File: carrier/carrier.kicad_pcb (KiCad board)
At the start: 2 copper layers, 14 x 12 mm, 2 parts, among them J1 DF40GB-30DP-0.4V(51), U1 TC58NVG1S3HBAI6

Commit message: Align net class + docs with the net names actually used
Schematic uses the datasheet slash form (/CE, /WE, /RE, /WP, RY//BY) rather
than the nCE-style placeholders I had documented. Signal class updated to
match; net-to-class patterns documented for manual entry.

Co-Authored-By: Claude Opus 5 <noreply@anthropic.com>
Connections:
- net /ALE renamed ALE
- net /CLE renamed CLE
- net /IO1 renamed IO1
- net /IO2 renamed IO2
- net /IO3 renamed IO3
- net /IO4 renamed IO4
- net /IO5 renamed IO5
- net /IO6 renamed IO6
- net /IO7 renamed IO7
- net /IO8 renamed IO8
- net /RY//BY renamed RY//BY
- net //CE renamed /CE
- net //RE renamed /RE
- net //WE renamed /WE
- net //WP renamed /WP
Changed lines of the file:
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@@
 			(size 0.23 0.66)
 			(layers "F.Cu" "F.Mask" "F.Paste")
-			(net "/IO1")
+			(net "IO1")
 			(pinfunction "1_1")
 			(pintype "passive")
@@
 			(size 0.23 0.66)
 			(layers "F.Cu" "F.Mask" "F.Paste")
-			(net "/{slash}CE")
+			(net "{slash}CE")
 			(pinfunction "4_4")
 			(pintype "passive")
@@
 			(size 0.23 0.66)
 			(layers "F.Cu" "F.Mask" "F.Paste")
-			(net "/IO2")
+			(net "IO2")
 			(pinfunction "5_5")
 			(pintype "passive")
@@
 			(size 0.23 0.66)
 			(layers "F.Cu" "F.Mask" "F.Paste")
-			(net "/CLE")
+			(net "CLE")
 			(pinfunction "8_8")
 			(pintype "passive")
@@
 			(size 0.23 0.66)
 			(layers "F.Cu" "F.Mask" "F.Paste")
-			(net "/IO3")
+			(net "IO3")
 			(pinfunction "9_9")
 			(pintype "passive")
@@
 			(size 0.23 0.66)
 			(layers "F.Cu" "F.Mask" "F.Paste")
-			(net "/ALE")
+			(net "ALE")
 			(pinfunction "12_12")
 			(pintype "passive")
@@
 			(size 0.23 0.66)
 			(layers "F.Cu" "F.Mask" "F.Paste")
-			(net "/IO4")
+			(net "IO4")
 			(pinfunction "13_13")
 			(pintype "passive")
@@
 			(size 0.23 0.66)
 			(layers "F.Cu" "F.Mask" "F.Paste")
-			(net "/{slash}WE")
+			(net "{slash}WE")
 			(pinfunction "16_16")
 			(pintype "passive")
@@
 			(size 0.23 0.66)
 			(layers "F.Cu" "F.Mask" "F.Paste")
-			(net "/IO5")
+			(net "IO5")
 			(pinfunction "17_17")
 			(pintype "passive")
@@
 			(size 0.23 0.66)
 			(layers "F.Cu" "F.Mask" "F.Paste")
-			(net "/{slash}RE")
+			(net "{slash}RE")
 			(pinfunction "20_20")
 			(pintype "passive")
@@
 			(size 0.23 0.66)
 			(layers "F.Cu" "F.Mask" "F.Paste")
-			(net "/IO6")
+			(net "IO6")
 			(pinfunction "21_21")
 			(pintype "passive")
@@
 			(size 0.23 0.66)
 			(layers "F.Cu" "F.Mask" "F.Paste")
-			(net "/{slash}WP")
+			(net "{slash}WP")
 			(pinfunction "24_24")
 			(pintype "passive")
@@
 			(size 0.23 0.66)
 			(layers "F.Cu" "F.Mask" "F.Paste")
-			(net "/IO7")
+			(net "IO7")
 			(pinfunction "25_25")
 			(pintype "passive")
@@
 			(size 0.23 0.66)
 			(layers "F.Cu" "F.Mask" "F.Paste")
-			(net "/RY{slash}{slash}BY")
+			(net "RY{slash}{slash}BY")
 			(pinfunction "28_28")
 			(pintype "passive")
@@
 			(size 0.23 0.66)
 			(layers "F.Cu" "F.Mask" "F.Paste")
-			(net "/IO8")
+			(net "IO8")
 			(pinfunction "29_29")
 			(pintype "passive")
@@
 			(size 0.4 0.4)
 			(layers "B.Cu" "B.Mask")
-			(net "/{slash}WP")
+			(net "{slash}WP")
 			(pinfunction "~{WP}_B2")
 			(pintype "input")
@@
 			(size 0.4 0.4)
 			(layers "B.Cu" "B.Mask")
-			(net "/ALE")
+			(net "ALE")
 			(pinfunction "ALE_B3")
 			(pintype "input")
@@
 			(size 0.4 0.4)
 			(layers "B.Cu" "B.Mask")
-			(net "/{slash}CE")
+			(net "{slash}CE")
 			(pinfunction "~{CE}_B5")
 			(pintype "input")
@@
 			(size 0.4 0.4)
 			(layers "B.Cu" "B.Mask")
-			(net "/{slash}WE")
+			(net "{slash}WE")
 			(pinfunction "~{WE}_B6")
 			(pintype "input")
@@
 			(size 0.4 0.4)
 			(layers "B.Cu" "B.Mask")
-			(net "/RY{slash}{slash}BY")
+			(net "RY{slash}{slash}BY")
 			(pinfunction "RY/~{BY}_B7")
 			(pintype "open_collector")
@@
 			(size 0.4 0.4)
 			(layers "B.Cu" "B.Mask")
-			(net "/{slash}RE")
+			(net "{slash}RE")
 			(pinfunction "~{RE}_C3")
 			(pintype "input")
@@
 			(size 0.4 0.4)
 			(layers "B.Cu" "B.Mask")
-			(net "/CLE")
+			(net "CLE")
 			(pinfunction "CLE_C4")
 			(pintype "input")
@@
 			(size 0.4 0.4)
 			(layers "B.Cu" "B.Mask")
-			(net "/IO1")
+			(net "IO1")
 			(pinfunction "I/O1_G3")
 			(pintype "bidirectional")
@@
 			(size 0.4 0.4)
 			(layers "B.Cu" "B.Mask")
-			(net "/IO2")
+			(net "IO2")
 			(pinfunction "I/O2_H3")
 			(pintype "bidirectional")
@@
 			(size 0.4 0.4)
 			(layers "B.Cu" "B.Mask")
-			(net "/IO6")
+			(net "IO6")
 			(pinfunction "I/O6_H6")
 			(pintype "bidirectional")
@@
 			(size 0.4 0.4)
 			(layers "B.Cu" "B.Mask")
-			(net "/IO8")
+			(net "IO8")
 			(pinfunction "I/O8_H7")
 			(pintype "bidirectional")
@@
 			(size 0.4 0.4)
 			(layers "B.Cu" "B.Mask")
-			(net "/IO3")
+			(net "IO3")
 			(pinfunction "I/O3_J3")
 			(pintype "bidirectional")
@@
 			(size 0.4 0.4)
 			(layers "B.Cu" "B.Mask")
-			(net "/IO4")
+			(net "IO4")
 			(pinfunction "I/O4_J4")
 			(pintype "bidirectional")
@@
 			(size 0.4 0.4)
 			(layers "B.Cu" "B.Mask")
-			(net "/IO5")
+			(net "IO5")
 			(pinfunction "I/O5_J5")
 			(pintype "bidirectional")
@@
 			(size 0.4 0.4)
 			(layers "B.Cu" "B.Mask")
-			(net "/IO7")
+			(net "IO7")
 			(pinfunction "I/O7_J6")
 			(pintype "bidirectional")

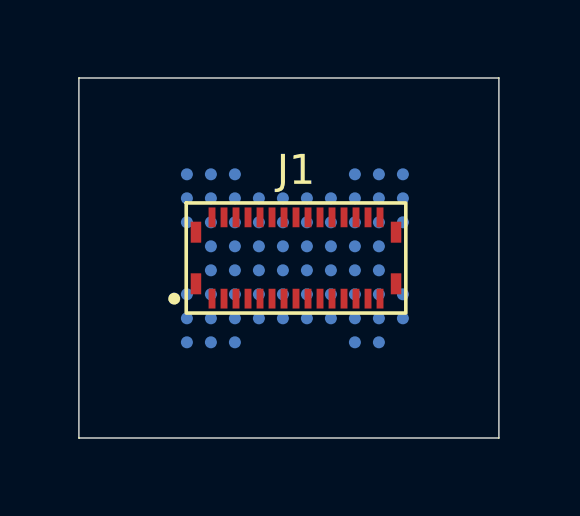
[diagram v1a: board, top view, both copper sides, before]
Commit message: Drop net class clearance to 0.1mm for the BGA escape
0.15mm clearance made the ball field unroutable: a 0.45mm dogbone via sits
0.1407mm from the neighbouring pad, and a 0.15mm trace between two pads
needs 0.45mm of the 0.40mm available. 0.1mm clears both with margin and is
still well above JLC's 0.09mm floor.

Default now carries the signal geometry so most nets need no pattern.

Co-Authored-By: Claude Opus 5 <noreply@anthropic.com>
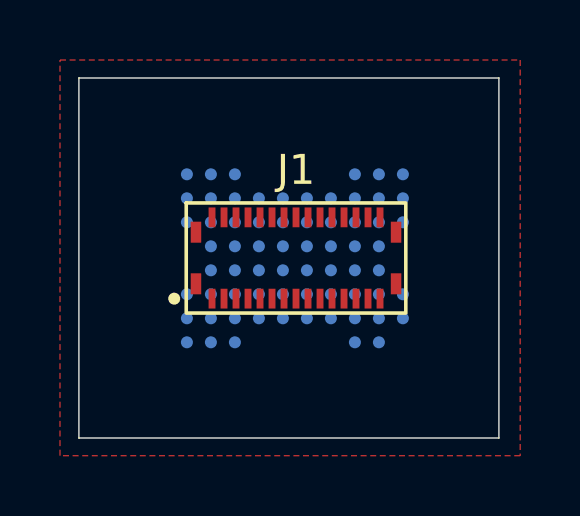
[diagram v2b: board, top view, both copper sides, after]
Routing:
- added copper zone on F.Cu, net GND
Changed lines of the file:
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@@
 		(capping no)
 		(filling no)
+		(zone_defaults)
 		(aux_axis_origin 178.51 108.77)
 		(pcbplotparams
@@
 		)
 		(solder_mask_margin 0.05)
-		(clearance 0.1)
 		(attr smd exclude_from_pos_files exclude_from_bom)
 		(duplicate_pad_numbers_are_jumpers no)
@@
 		(layer "Edge.Cuts")
 	)
+	(zone
+		(net "GND")
+		(layer "F.Cu")
+		(name "GND")
+		(hatch edge 0.5)
+		(connect_pads yes
+			(clearance 0.5)
+		)
+		(min_thickness 0.25)
+		(fill yes
+			(thermal_gap 0.5)
+			(thermal_bridge_width 0.5)
+			(island_removal_mode 0)
+		)
+		(polygon
+			(pts
+				(xy 177.88 96.17) (xy 193.22 96.17) (xy 193.22 109.36) (xy 177.88 109.36)
+			)
+		)
+	)
 	(embedded_fonts no)

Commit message: Carrier: import nets, go 4-layer, fix netclass patterns
carrier.kicad_pcb (equivalent of Update PCB from Schematic):
- U1 fpid bga67-to-dip: -> carrier:
- 17 nets imported, all 101 pads assigned, matching the schematic
  netlist pad for pad
- 4 copper layers on a JLCPCB 1.6 mm 4-layer stackup
  (1 oz outer / 0.5 oz inner, 0.2104 prepreg / 1.065 core)
- GND pour moved off F.Cu to In1.Cu

U1 stays on B.Cu and J1 on F.Cu: F.Cu is the mating face.

Net class patterns: root-sheet local labels land on the board as
"/IO1", "/{slash}CE" and so on, so the documented "IO*" pattern matched
nothing and all 15 signal nets fell through to Default. Replaced with
"/*" -> Signal, which now resolves correctly. VCC and GND come from
power symbols, are global, and stay unprefixed.

base: 4 copper layers; net classes and patterns aligned with carrier,
which is what docs/HANDOFF.md already claimed was true.

DRC: 0 violations, 37 unconnected items (nothing routed yet).

Co-Authored-By: Claude Opus 5 <noreply@anthropic.com>
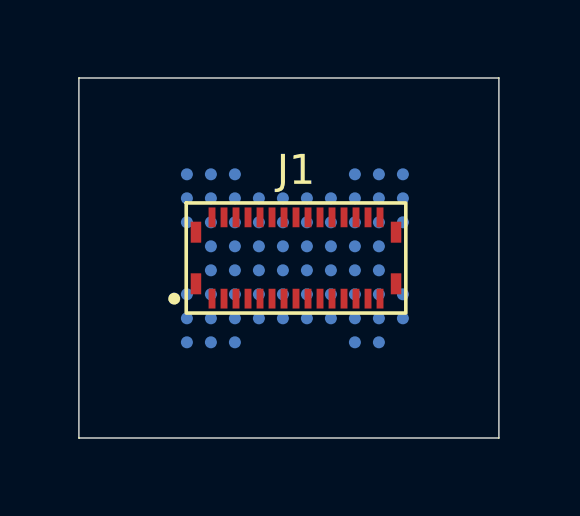
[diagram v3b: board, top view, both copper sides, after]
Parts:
- U1: footprint bga67-to-dip:BGA-67_6.5x8.0mm_Layout8x10_P0.8mm -> carrier:BGA-67_6.5x8.0mm_Layout8x10_P0.8mm
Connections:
- net ALE renamed /ALE
- net CLE renamed /CLE
- net IO1 renamed /IO1
- net IO2 renamed /IO2
- net IO3 renamed /IO3
- net IO4 renamed /IO4
- net IO5 renamed /IO5
- net IO6 renamed /IO6
- net IO7 renamed /IO7
- net IO8 renamed /IO8
- net RY//BY renamed /RY//BY
- net /CE renamed //CE
- net /RE renamed //RE
- net /WE renamed //WE
- net /WP renamed //WP
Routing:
- added copper zone on In1.Cu, net GND
- removed copper zone on F.Cu, net GND
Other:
- copper layers 2 -> 4
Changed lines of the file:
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@@
 	(layers
 		(0 "F.Cu" signal)
+		(4 "In1.Cu" signal)
+		(6 "In2.Cu" signal)
 		(2 "B.Cu" signal)
 		(9 "F.Adhes" user "F.Adhesive")
@@
 			)
 			(layer "dielectric 1"
+				(type "prepreg")
+				(thickness 0.2104)
+				(material "FR4")
+				(epsilon_r 4.5)
+				(loss_tangent 0.02)
+			)
+			(layer "In1.Cu"
+				(type "copper")
+				(thickness 0.0152)
+			)
+			(layer "dielectric 2"
 				(type "core")
-				(thickness 1.51)
+				(thickness 1.065)
+				(material "FR4")
+				(epsilon_r 4.5)
+				(loss_tangent 0.02)
+			)
+			(layer "In2.Cu"
+				(type "copper")
+				(thickness 0.0152)
+			)
+			(layer "dielectric 3"
+				(type "prepreg")
+				(thickness 0.2104)
 				(material "FR4")
 				(epsilon_r 4.5)
@@
 		(capping no)
 		(filling no)
-		(zone_defaults)
 		(aux_axis_origin 178.51 108.77)
 		(pcbplotparams
@@
 			(size 0.23 0.66)
 			(layers "F.Cu" "F.Mask" "F.Paste")
-			(net "IO1")
+			(net "/IO1")
 			(pinfunction "1_1")
 			(pintype "passive")
@@
 			(size 0.23 0.66)
 			(layers "F.Cu" "F.Mask" "F.Paste")
-			(net "{slash}CE")
+			(net "/{slash}CE")
 			(pinfunction "4_4")
 			(pintype "passive")
@@
 			(size 0.23 0.66)
 			(layers "F.Cu" "F.Mask" "F.Paste")
-			(net "IO2")
+			(net "/IO2")
 			(pinfunction "5_5")
 			(pintype "passive")
@@
 			(size 0.23 0.66)
 			(layers "F.Cu" "F.Mask" "F.Paste")
-			(net "CLE")
+			(net "/CLE")
 			(pinfunction "8_8")
 			(pintype "passive")
@@
 			(size 0.23 0.66)
 			(layers "F.Cu" "F.Mask" "F.Paste")
-			(net "IO3")
+			(net "/IO3")
 			(pinfunction "9_9")
 			(pintype "passive")
@@
 			(size 0.23 0.66)
 			(layers "F.Cu" "F.Mask" "F.Paste")
-			(net "ALE")
+			(net "/ALE")
 			(pinfunction "12_12")
 			(pintype "passive")
@@
 			(size 0.23 0.66)
 			(layers "F.Cu" "F.Mask" "F.Paste")
-			(net "IO4")
+			(net "/IO4")
 			(pinfunction "13_13")
 			(pintype "passive")
@@
 			(size 0.23 0.66)
 			(layers "F.Cu" "F.Mask" "F.Paste")
-			(net "{slash}WE")
+			(net "/{slash}WE")
 			(pinfunction "16_16")
 			(pintype "passive")
@@
 			(size 0.23 0.66)
 			(layers "F.Cu" "F.Mask" "F.Paste")
-			(net "IO5")
+			(net "/IO5")
 			(pinfunction "17_17")
 			(pintype "passive")
@@
 			(size 0.23 0.66)
 			(layers "F.Cu" "F.Mask" "F.Paste")
-			(net "{slash}RE")
+			(net "/{slash}RE")
 			(pinfunction "20_20")
 			(pintype "passive")
@@
 			(size 0.23 0.66)
 			(layers "F.Cu" "F.Mask" "F.Paste")
-			(net "IO6")
+			(net "/IO6")
 			(pinfunction "21_21")
 			(pintype "passive")
@@
 			(size 0.23 0.66)
 			(layers "F.Cu" "F.Mask" "F.Paste")
-			(net "{slash}WP")
+			(net "/{slash}WP")
 			(pinfunction "24_24")
 			(pintype "passive")
@@
 			(size 0.23 0.66)
 			(layers "F.Cu" "F.Mask" "F.Paste")
-			(net "IO7")
+			(net "/IO7")
 			(pinfunction "25_25")
 			(pintype "passive")
@@
 			(size 0.23 0.66)
 			(layers "F.Cu" "F.Mask" "F.Paste")
-			(net "RY{slash}{slash}BY")
+			(net "/RY{slash}{slash}BY")
 			(pinfunction "28_28")
 			(pintype "passive")
@@
 			(size 0.23 0.66)
 			(layers "F.Cu" "F.Mask" "F.Paste")
-			(net "IO8")
+			(net "/IO8")
 			(pinfunction "29_29")
 			(pintype "passive")
@@
 		(embedded_fonts no)
 	)
-	(footprint "bga67-to-dip:BGA-67_6.5x8.0mm_Layout8x10_P0.8mm"
+	(footprint "carrier:BGA-67_6.5x8.0mm_Layout8x10_P0.8mm"
 		(layer "B.Cu")
 		(at 185.71 102.78 90)
@@
 			(size 0.4 0.4)
 			(layers "B.Cu" "B.Mask")
-			(net "{slash}WP")
+			(net "/{slash}WP")
 			(pinfunction "~{WP}_B2")
 			(pintype "input")
@@
 			(size 0.4 0.4)
 			(layers "B.Cu" "B.Mask")
-			(net "ALE")
+			(net "/ALE")
 			(pinfunction "ALE_B3")
 			(pintype "input")
@@
 			(size 0.4 0.4)
 			(layers "B.Cu" "B.Mask")
-			(net "{slash}CE")
+			(net "/{slash}CE")
 			(pinfunction "~{CE}_B5")
 			(pintype "input")
@@
 			(size 0.4 0.4)
 			(layers "B.Cu" "B.Mask")
-			(net "{slash}WE")
+			(net "/{slash}WE")
 			(pinfunction "~{WE}_B6")
 			(pintype "input")
@@
 			(size 0.4 0.4)
 			(layers "B.Cu" "B.Mask")
-			(net "RY{slash}{slash}BY")
+			(net "/RY{slash}{slash}BY")
 			(pinfunction "RY/~{BY}_B7")
 			(pintype "open_collector")
@@
 			(size 0.4 0.4)
 			(layers "B.Cu" "B.Mask")
-			(net "{slash}RE")
+			(net "/{slash}RE")
 			(pinfunction "~{RE}_C3")
 			(pintype "input")
@@
 			(size 0.4 0.4)
 			(layers "B.Cu" "B.Mask")
-			(net "CLE")
+			(net "/CLE")
 			(pinfunction "CLE_C4")
 			(pintype "input")
@@
 			(size 0.4 0.4)
 			(layers "B.Cu" "B.Mask")
-			(net "IO1")
+			(net "/IO1")
 			(pinfunction "I/O1_G3")
 			(pintype "bidirectional")
@@
 			(size 0.4 0.4)
 			(layers "B.Cu" "B.Mask")
-			(net "IO2")
+			(net "/IO2")
 			(pinfunction "I/O2_H3")
 			(pintype "bidirectional")
@@
 			(size 0.4 0.4)
 			(layers "B.Cu" "B.Mask")
-			(net "IO6")
+			(net "/IO6")
 			(pinfunction "I/O6_H6")
 			(pintype "bidirectional")
@@
 			(size 0.4 0.4)
 			(layers "B.Cu" "B.Mask")
-			(net "IO8")
+			(net "/IO8")
 			(pinfunction "I/O8_H7")
 			(pintype "bidirectional")
@@
 			(size 0.4 0.4)
 			(layers "B.Cu" "B.Mask")
-			(net "IO3")
+			(net "/IO3")
 			(pinfunction "I/O3_J3")
 			(pintype "bidirectional")
@@
 			(size 0.4 0.4)
 			(layers "B.Cu" "B.Mask")
-			(net "IO4")
+			(net "/IO4")
 			(pinfunction "I/O4_J4")
 			(pintype "bidirectional")
@@
 			(size 0.4 0.4)
 			(layers "B.Cu" "B.Mask")
-			(net "IO5")
+			(net "/IO5")
 			(pinfunction "I/O5_J5")
 			(pintype "bidirectional")
@@
 			(size 0.4 0.4)
 			(layers "B.Cu" "B.Mask")
-			(net "IO7")
+			(net "/IO7")
 			(pinfunction "I/O7_J6")
 			(pintype "bidirectional")
@@
 	(zone
 		(net "GND")
-		(layer "F.Cu")
+		(layer "In1.Cu")
 		(name "GND")
 		(hatch edge 0.5)
@@
 		)
 		(min_thickness 0.25)
-		(fill yes
+		(fill
 			(thermal_gap 0.5)
 			(thermal_bridge_width 0.5)

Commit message: GND plane to In2.Cu; add DF40 30-pin plug to the library
The ball field is on B.Cu, so the adjacent inner layer is In2.Cu (L3),
not In1.Cu. Moved the pour there. DRC still clean, 37 unconnected.

DF40GB-30DP-0.4V(51) existed only in the schematic's lib_symbols cache,
so board B could not reference it and "Update Symbols from Library"
would have dropped it. Copied into lib/carrier.kicad_sym. All three
library symbols parse and plot.

Co-Authored-By: Claude Opus 5 <noreply@anthropic.com>
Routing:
- added copper zone on In2.Cu, net GND
- removed copper zone on In1.Cu, net GND
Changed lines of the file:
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@@
 	(zone
 		(net "GND")
-		(layer "In1.Cu")
+		(layer "In2.Cu")
 		(name "GND")
 		(hatch edge 0.5)

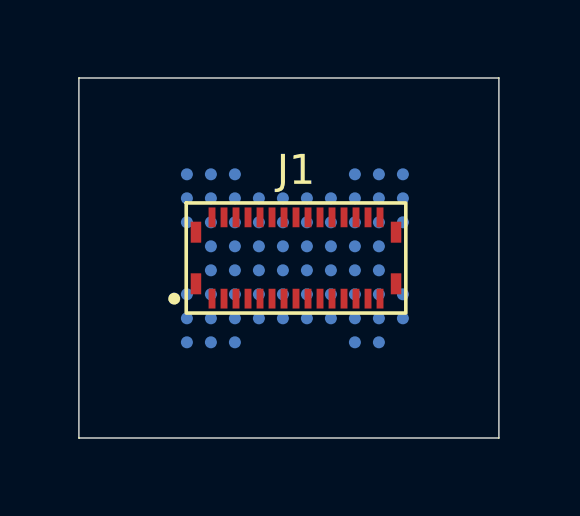
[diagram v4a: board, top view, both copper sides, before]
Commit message: carrier: place U1/J1 and escape all 67-ball nets
Placement. Scored all four U1 rotations against both J1 rotations by
counting straight-line crossings between matching pads. U1 at 90 with
J1 at 180 gives 4 crossings over 46 mm; the as-drawn U1 90 / J1 0 gives
19 over 51 mm. Both parts centred on the board - U1 was 0.2 mm off in X.

Escape. The BGA's diagonal-midpoint lattice is a usable routing grid on
B.Cu: a trace running between two pad columns clears them by 0.125 mm
and a node sits 0.5657 mm from four pads. Routed all 20 netted balls on
that lattice with a maze router, most-constrained ball first, avoiding
nodes that are another ball's last remaining escape. 20/20 escaped, 29
B.Cu tracks, 20 vias. Rows A, D, E, F and K are entirely NC and are left
untouched.

Vias are 0.45 / 0.20, not the 0.45 / 0.25 the earlier analysis implies.
Copper clearance is not the binding constraint - hole clearance is, and
it is measured from the drill: a 0.25 mm drill lands 0.2407 mm from the
ball pads against a 0.25 mm rule, which is 72 errors. 0.20 mm gives
0.2657 mm and keeps a 0.125 mm annular ring.

Also:
- min_copper_edge_clearance 0.5 -> 0.2, per JLCPCB capability. 0.5 costs
  a millimetre of usable width on a 14 mm board.
- Ground zone clearance 0.5 -> 0.2, thermal gap 0.5 -> 0.3, pads solid.
  At 0.5 every via punched a 1.45 mm hole and the plane under the ball
  field was shredded. In2.Cu is now continuous at 147.5 of 168 mm2.

DRC: 0 errors. The 17 dangling vias and 35 unconnected items are the J1
side, which is not routed yet.

Co-Authored-By: Claude Opus 5 <noreply@anthropic.com>
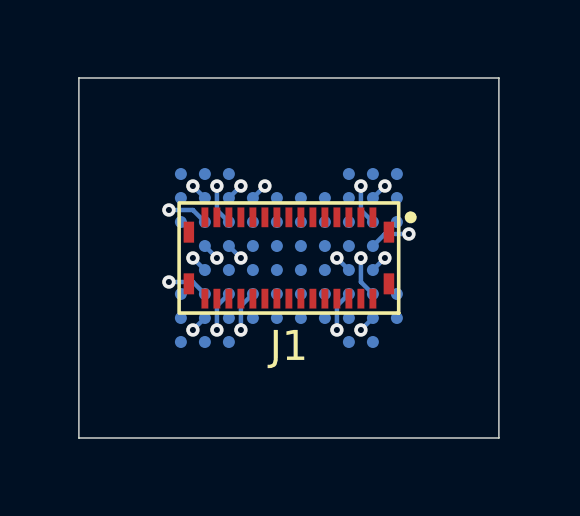
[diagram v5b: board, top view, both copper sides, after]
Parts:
- moved J1 0.24 mm to (185.5, 102.8), turned to 180 degrees
- moved U1 0.20 mm to (185.5, 102.8)
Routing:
- net GND: track 0.00 -> 1.70 mm, vias 0 -> 3
- net /IO3: track 0.00 -> 1.37 mm, vias 0 -> 1
- net /IO7: track 0.00 -> 1.37 mm, vias 0 -> 1
- net /IO1: track 0.00 -> 1.37 mm, vias 0 -> 1
- net /ALE: track 0.00 -> 1.37 mm, vias 0 -> 1
- net //WE: track 0.00 -> 1.37 mm, vias 0 -> 1
- net //CE: track 0.00 -> 1.37 mm, vias 0 -> 1
- net //RE: track 0.00 -> 1.37 mm, vias 0 -> 1
- net /IO2: track 0.00 -> 1.37 mm, vias 0 -> 1
- net /IO6: track 0.00 -> 1.37 mm, vias 0 -> 1
- net VCC: track 0.00 -> 1.13 mm, vias 0 -> 2
- net //WP: track 0.00 -> 0.57 mm, vias 0 -> 1
- net /IO4: track 0.00 -> 0.57 mm, vias 0 -> 1
- net /RY//BY: track 0.00 -> 0.57 mm, vias 0 -> 1
- net /IO8: track 0.00 -> 0.57 mm, vias 0 -> 1
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
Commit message: wip: hand routing on F.Cu, GND pours on all four layers
Alex's routing pass. 35 unconnected -> 10, 17 dangling vias -> 8.
Preserved before the pinout rework replaces it.

Co-Authored-By: Claude Opus 5 <noreply@anthropic.com>
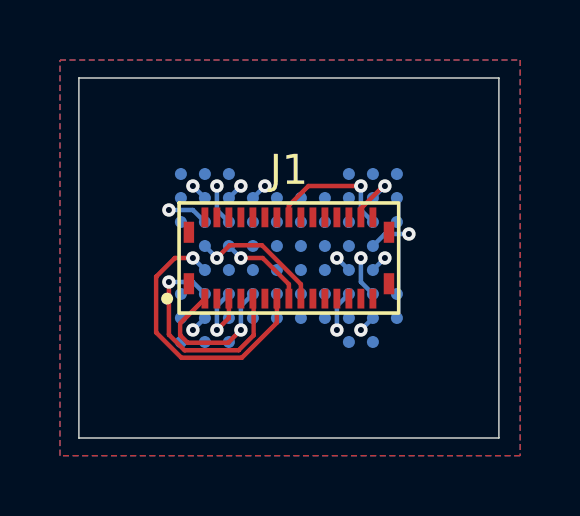
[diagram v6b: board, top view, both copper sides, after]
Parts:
- turned J1 to 0 degrees
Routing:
- net /IO4: track 0.57 -> 9.57 mm
- net /IO3: track 1.37 -> 7.60 mm
- net VCC: track 1.13 -> 6.31 mm
- net /IO5: track 0.57 -> 4.56 mm
- net /IO1: track 1.37 -> 5.23 mm
- net //WE: track 1.37 -> 4.43 mm
- net /RY//BY: track 0.57 -> 1.97 mm
- net /IO2: track 1.37 -> 2.58 mm
- added copper zone on B.Cu, net GND
- added copper zone on F.Cu, net GND
- added copper zone on In1.Cu, net GND
